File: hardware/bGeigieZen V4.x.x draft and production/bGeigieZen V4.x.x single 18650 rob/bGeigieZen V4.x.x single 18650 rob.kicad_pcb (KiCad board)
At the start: 2 copper layers, 129.4 x 64.6 mm, 13 parts, among them J1 M5 2x15 pin, J3 GPS, J4 Geiger Safepulse, J5 Extra support header

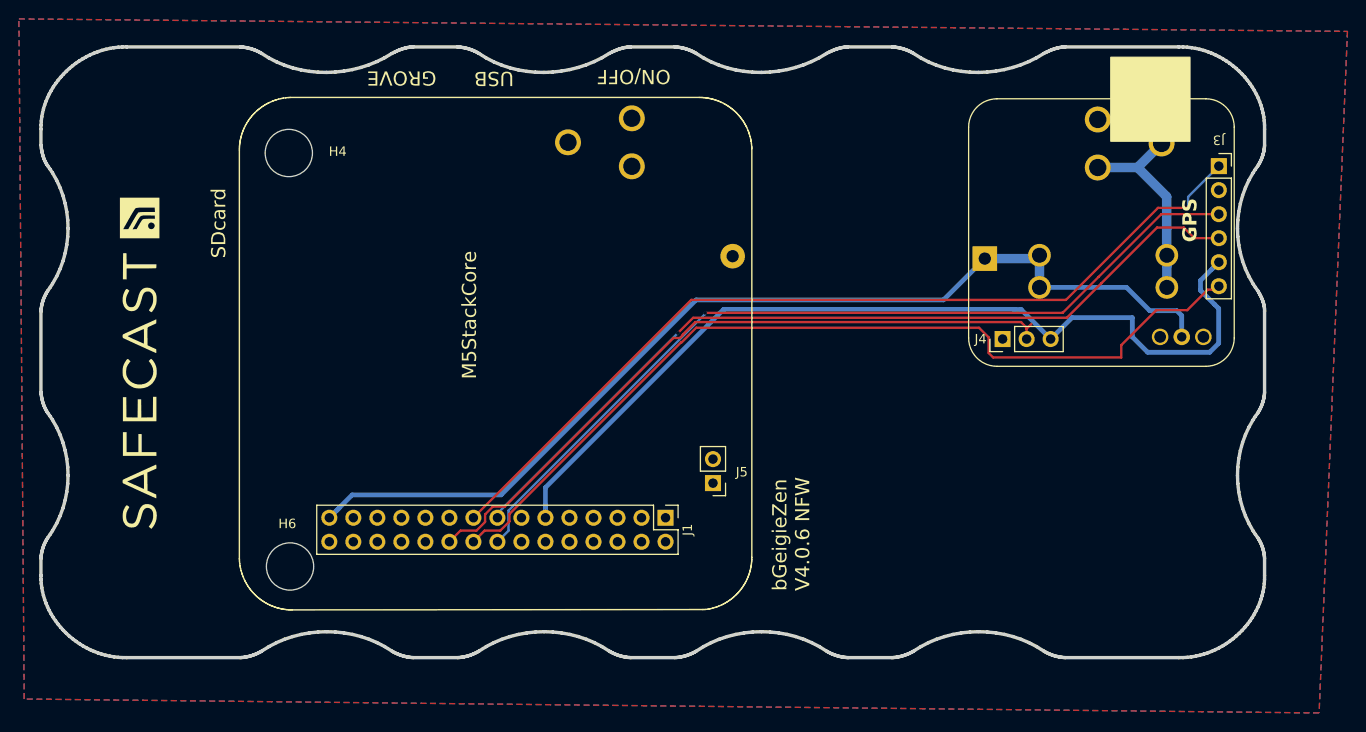
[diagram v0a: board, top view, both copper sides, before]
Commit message: Updated boards for Zen V4.0.7
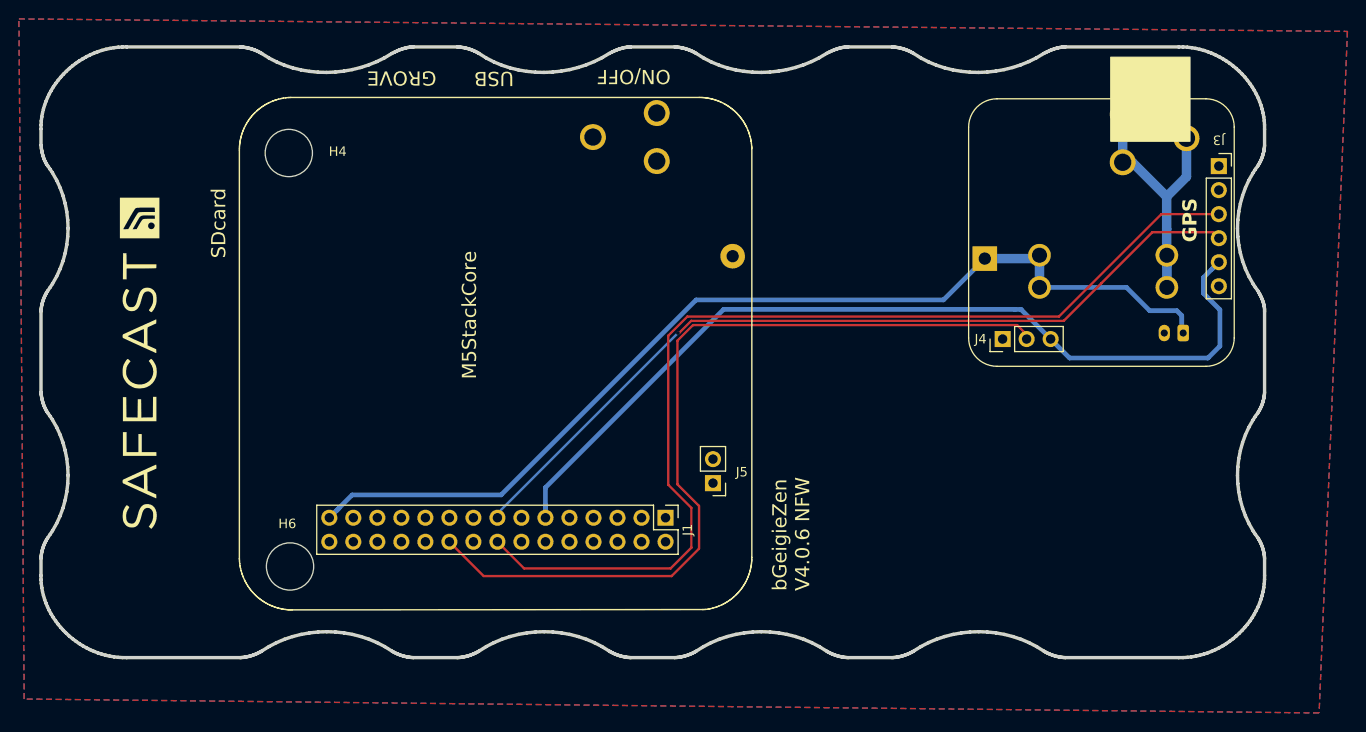
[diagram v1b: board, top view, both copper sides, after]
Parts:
- removed QI charger: QI GND, Connector_JST:JST_PH_B2B-PH-K_1x02_P2.00mm_Vertical
- added QIcharger1: QI GND, Connector_JST:JST_PH_B2B-PH-K_1x02_P2.00mm_Vertical, B.Cu at (205.4, 96.9)
- moved G*** 3.27 mm to (169.0, 76.8)
- moved BT1 2.70 mm to (175.1, 76.3)
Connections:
- J1 pad 17: /SDA -> unconnected-(J1-Pin_17-Pad17)
- J1 pad 18: /SCL -> unconnected-(J1-Pin_18-Pad18)
- J3 pad 1: /SDA -> unconnected-(J3-Pin_1-Pad1)
- J3 pad 6: /SCL -> unconnected-(J3-Pin_6-Pad6)
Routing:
- net /SCL: track 95.8 -> 0.00 mm
- net /SDA: track 95.1 -> 0.00 mm, vias 1 -> 0
- net /GIO2 on Core and GIO32 on Core-2: track 72.5 -> 91.1 mm
- net /TX2: track 91.1 -> 109.6 mm, vias 1 -> 0
- net 3.3V: track 100.0 -> 97.6 mm
- net Net-(BT1-+): track 32.9 -> 30.7 mm
- net unconnected-(J1-Pin_18-Pad18): track 0.00 -> 1.69 mm
- net unconnected-(J3-Pin_6-Pad6): track 0.00 -> 0.52 mm

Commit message: Updated 3D models sizes
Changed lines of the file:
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@@
 		(model "${KIPRJMOD}/shapes3D/lnd7318-2.wrl"
 			(offset
-				(xyz -15.5 -32.5 -9)
+				(xyz -17 -34 -9)
 			)
 			(scale
-				(xyz 3.5 3.5 3.5)
+				(xyz 3.9 3.9 3.9)
 			)
 			(rotate
-				(xyz 90 0 -125)
+				(xyz 90 -0 -125)
 			)
 		)
 		(model "${KIPRJMOD}/shapes3D/grid cover.wrl"
 			(offset
-				(xyz -15 -32.5 -16)
+				(xyz -17 -34 -16)
 			)
 			(scale
-				(xyz 0.32 0.32 0.32)
+				(xyz 0.38 0.38 0.38)
 			)
 			(rotate
-				(xyz 0 -180 55)
+				(xyz -0 -180 55)
 			)
 		)
@@
 	)
 	(gr_rect
-		(start 197.724724 67.751456)
-		(end 206.106724 76.641456)
+		(start 202.1078 69.2684)
+		(end 210.4898 74.2684)
 		(locked yes)
 		(stroke

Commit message: Added 3d update 3dModel of tube grid and update boards
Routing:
- net /BAT: track 109.7 -> 109.2 mm
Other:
- board text added: "bGeigieZen V4.0.7 NFW"
- board text removed: "bGeigieZen V4.0.6 NFW"
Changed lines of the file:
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@@
 (kicad_pcb
-	(version 20240703)
+	(version 20240706)
 	(generator "pcbnew")
 	(generator_version "8.99")
@@
 	(paper "A4")
 	(title_block
-		(title "bGeigieZen Draft V4.0.6 NFW")
-		(date "2024-06-20")
-		(rev "V4.0.6 rob")
+		(title "bGeigieZen Draft V4.0.7 NFW")
+		(date "2024-07-27")
+		(rev "V4.0.7 rob")
 		(comment 1 "Not For Whimps version.")
 	)
@@
 			(layer "F.SilkS")
 		)
+		(embedded_fonts no)
 	)
 	(footprint "Connector_PinHeader_2.54mm:PinHeader_2x15_P2.54mm_Vertical"
@@
 			(pintype "passive")
 		)
+		(embedded_fonts no)
 		(model "${KICAD6_3DMODEL_DIR}/Connector_PinHeader_2.54mm.3dshapes/PinHeader_2x15_P2.54mm_Vertical.wrl"
 			(offset
@@
 			(pintype "passive")
 		)
+		(embedded_fonts no)
 		(model "${KICAD8_3DMODEL_DIR}/Connector_PinHeader_2.54mm.3dshapes/PinHeader_1x06_P2.54mm_Vertical.step"
 			(offset
@@
 			(layers "F&B.Cu" "*.Mask")
 		)
+		(embedded_fonts no)
 	)
 	(footprint "Connector_PinHeader_2.54mm:PinHeader_1x02_P2.54mm_Vertical"
@@
 			(pintype "passive")
 		)
+		(embedded_fonts no)
 		(model "${KICAD6_3DMODEL_DIR}/Connector_PinHeader_2.54mm.3dshapes/PinHeader_1x02_P2.54mm_Vertical.wrl"
 			(hide yes)
@@
 			(pintype "passive")
 		)
+		(embedded_fonts no)
 		(model "${KICAD6_3DMODEL_DIR}/Connector_PinHeader_2.54mm.3dshapes/PinHeader_1x03_P2.54mm_Vertical.wrl"
 			(hide yes)
@@
 			(layers "F&B.Cu" "*.Mask")
 		)
+		(embedded_fonts no)
 	)
 	(footprint "Diode_THT:D_DO-201_P15.24mm_Horizontal"
@@
 			(pintype "passive")
 		)
+		(embedded_fonts no)
 		(model "${KICAD8_3DMODEL_DIR}/Diode_THT.3dshapes/D_DO-201_P15.24mm_Horizontal.wrl"
 			(offset
@@
 			)
 		)
+		(embedded_fonts no)
 	)
 	(footprint "Library:BATTERY_18650-HOLDER"
@@
 			(net 1 "GND")
 		)
+		(embedded_fonts no)
 		(model "${KIPRJMOD}/shapes3D/KEYELCO_54.wrl"
 			(offset
@@
 			(solder_mask_margin 0.102)
 		)
+		(embedded_fonts no)
 		(model "${KIPRJMOD}/shapes3D/Fuse - mini 10A v005.wrl"
 			(offset
@@
 			(layer "B.SilkS")
 		)
+		(embedded_fonts no)
 	)
 	(footprint "Connector_JST:JST_PH_B2B-PH-K_1x02_P2.00mm_Vertical"
@@
 			(pintype "passive")
 		)
+		(embedded_fonts no)
 		(model "${KICAD8_3DMODEL_DIR}/Connector_JST.3dshapes/JST_PH_B2B-PH-K_1x02_P2.00mm_Vertical.wrl"
 			(offset
@@
 		(layer "Edge.Cuts")
 	)
-	(gr_text "bGeigieZen\nV4.0.6 NFW"
+	(gr_text "bGeigieZen\nV4.0.7 NFW"
 		(at 200.5584 112.724 90)
 		(layer "B.SilkS")
@@
 		)
 	)
-	(gr_text "bGeigieZen\nV4.0.6 NFW\n"
+	(gr_text "bGeigieZen\nV4.0.7 NFW\n"
 		(at 163.9316 124.2048 90)
 		(layer "F.SilkS")
@@
 	)
 	(segment
-		(start 209.155 86.9507)
-		(end 209.155 87.0096)
+		(start 196.704 91.6855)
+		(end 192.7543 95.6352)
 		(width 0.25)
 		(layer "F.Cu")
@@
 	)
 	(segment
-		(start 209.155 86.9065)
-		(end 209.155 86.8991)
+		(start 209.155 86.9507)
+		(end 209.155 87.0096)
 		(width 0.25)
 		(layer "F.Cu")
@@
 	)
 	(segment
-		(start 202.1323 86.2572)
-		(end 208.5186 86.2572)
+		(start 153.2328 95.6352)
+		(end 151.943 96.925)
 		(width 0.25)
 		(layer "F.Cu")
@@
 	)
 	(segment
-		(start 152.068404 96.9252)
-		(end 151.943 96.9252)
+		(start 209.155 86.9065)
+		(end 209.155 86.8991)
 		(width 0.25)
 		(layer "F.Cu")
@@
 	)
 	(segment
+		(start 208.2034 86.8918)
+		(end 207.5688 86.2572)
+		(width 0.25)
+		(layer "F.Cu")
+		(net 2)
+	)
+	(segment
+		(start 202.1323 86.2572)
+		(end 196.704 91.6855)
+		(width 0.25)
+		(layer "F.Cu")
+		(net 2)
+	)
+	(segment
 		(start 209.155 86.9212)
 		(end 209.155 86.9065)
@@
 	)
 	(segment
-		(start 209.1551 86.8935)
-		(end 209.1551 86.8918)
+		(start 151.943 96.925)
+		(end 151.943 96.9252)
 		(width 0.25)
 		(layer "F.Cu")
@@
 	)
 	(segment
-		(start 196.704 91.6855)
-		(end 192.7543 95.6352)
+		(start 192.7543 95.6352)
+		(end 153.2328 95.6352)
+		(width 0.25)
+		(layer "F.Cu")
+		(net 2)
+	)
+	(segment
+		(start 209.1551 86.8935)
+		(end 209.1551 86.8918)
 		(width 0.25)
 		(layer "F.Cu")
@@
 	)
 	(segment
-		(start 153.358404 95.6352)
-		(end 152.068404 96.9252)
+		(start 209.155 86.8936)
+		(end 209.155 86.8954)
 		(width 0.25)
 		(layer "F.Cu")
@@
 	(segment
 		(start 209.155 86.8936)
-		(end 209.155 86.8954)
+		(end 209.1551 86.8935)
 		(width 0.25)
 		(layer "F.Cu")
@@
 	)
 	(segment
-		(start 196.748 91.642)
-		(end 196.704 91.6855)
+		(start 207.5688 86.2572)
+		(end 202.1323 86.2572)
 		(width 0.25)
 		(layer "F.Cu")
@@
 	)
 	(segment
-		(start 209.155 86.8936)
-		(end 209.1551 86.8935)
+		(start 209.1551 86.8918)
+		(end 208.2034 86.8918)
 		(width 0.25)
 		(layer "F.Cu")
@@
 	)
 	(segment
-		(start 192.7543 95.6352)
-		(end 153.358404 95.6352)
-		(width 0.25)
-		(layer "F.Cu")
-		(net 2)
-	)
-	(segment
-		(start 196.704 91.6855)
-		(end 202.1323 86.2572)
-		(width 0.25)
-		(layer "F.Cu")
-		(net 2)
-	)
-	(segment
 		(start 209.155 86.9507)
 		(end 209.155 86.9212)
@@
 		(net 2)
 	)
-	(segment
-		(start 208.5186 86.2572)
-		(end 209.155 86.8936)
-		(width 0.25)
-		(layer "F.Cu")
-		(net 2)
-	)
 	(via
 		(at 151.943 96.9252)
@@
 	)
 	(segment
-		(start 116.156 115.382)
-		(end 115.796 115.742)
-		(width 0.5)
-		(layer "B.Cu")
-		(net 27)
-	)
-	(segment
 		(start 133.2482 114.045)
 		(end 117.4929 114.045)
@@
 		)
 	)
+	(embedded_fonts no)
 )

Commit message: Some more small fixes on the V4.x.x NFW board
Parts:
- renumbered QIcharger1 to QI-charger
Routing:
- net Net-(BT1-+): track 30.7 -> 32.9 mm
- net /TX2: track 109.6 -> 110.7 mm
- net 3.3V: track 97.6 -> 96.7 mm
- net /GIO2 on Core and GIO32 on Core-2: track 91.1 -> 91.7 mm

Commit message: Updated boards
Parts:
- moved Fuse 2A 0.12 mm to (197.0, 90.4)
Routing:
- net Net-(BT1-+): track 32.9 -> 30.7 mm
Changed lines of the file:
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@@
 	(footprint "bGeigieZen:FUSE_3557-2"
 		(layer "B.Cu")
-		(at 196.9222 90.3992 180)
+		(at 197.0426 90.3992 180)
 		(property "Reference" "Fuse 2A"
 			(at 0.0722 -4.24 0)
@@
 		)
 		(pad "1" thru_hole circle
-			(at -6.735 -1.7 180)
-			(size 2.4 2.4)
-			(drill 1.6)
+			(at -7 -1.7 180)
+			(size 2.6 2.6)
+			(drill 1.8)
 			(layers "F&B.Cu" "*.Mask")
 			(remove_unused_layers no)
@@
 		)
 		(pad "1" thru_hole circle
-			(at -6.735 1.7 180)
-			(size 2.4 2.4)
-			(drill 1.6)
+			(at -7 1.7 180)
+			(size 2.6 2.6)
+			(drill 1.8)
 			(layers "F&B.Cu" "*.Mask")
 			(remove_unused_layers no)
@@
 		)
 		(pad "2" thru_hole circle
-			(at 6.735 -1.7 180)
-			(size 2.4 2.4)
-			(drill 1.6)
+			(at 7 -1.7 180)
+			(size 2.6 2.6)
+			(drill 1.8)
 			(layers "F&B.Cu" "*.Mask")
 			(remove_unused_layers no)
@@
 		)
 		(pad "2" thru_hole circle
-			(at 6.735 1.7 180)
-			(size 2.4 2.4)
-			(drill 1.6)
+			(at 7 1.7 180)
+			(size 2.6 2.6)
+			(drill 1.8)
 			(layers "F&B.Cu" "*.Mask")
 			(remove_unused_layers no)
@@
 	)
 	(segment
-		(start 203.657 88.7161)
-		(end 203.657 88.7076)
-		(width 0.5)
-		(layer "B.Cu")
-		(net 31)
-	)
-	(segment
-		(start 203.657 89.7863)
-		(end 203.657 89.2427)
-		(width 0.5)
-		(layer "B.Cu")
-		(net 31)
-	)
-	(segment
-		(start 205.736 78.3616)
-		(end 205.736 80.3974)
-		(width 1)
-		(layer "B.Cu")
-		(net 31)
-	)
-	(segment
-		(start 203.657 89.7865)
-		(end 203.657 89.7863)
+		(start 204.0426 92.0992)
+		(end 204.0426 88.6992)
 		(width 1)
 		(layer "B.Cu")
@@
 	)
 	(segment
-		(start 203.657 88.835)
-		(end 203.657 88.7671)
-		(width 0.5)
-		(layer "B.Cu")
-		(net 31)
-	)
-	(segment
 		(start 205.7356 78.3612)
 		(end 205.7356 76.3258)
@@
 	)
 	(segment
-		(start 203.657 88.7161)
-		(end 203.657 88.7076)
-		(width 1)
-		(layer "B.Cu")
-		(net 31)
-	)
-	(segment
-		(start 203.657 88.835)
-		(end 203.657 88.7671)
-		(width 1)
-		(layer "B.Cu")
-		(net 31)
-	)
-	(segment
-		(start 203.657 88.7331)
-		(end 203.657 88.7161)
-		(width 0.5)
-		(layer "B.Cu")
-		(net 31)
-	)
-	(segment
-		(start 203.636 85.899)
-		(end 203.636 82.497)
-		(width 1)
-		(layer "B.Cu")
-		(net 31)
-	)
-	(segment
-		(start 203.657 88.7076)
-		(end 203.657 88.6992)
-		(width 1)
-		(layer "B.Cu")
-		(net 31)
-	)
-	(segment
-		(start 203.657 88.7331)
-		(end 203.657 88.7161)
-		(width 1)
-		(layer "B.Cu")
-		(net 31)
-	)
-	(segment
-		(start 203.636 85.899)
-		(end 203.657 85.9202)
-		(width 0.5)
-		(layer "B.Cu")
-		(net 31)
-	)
-	(segment
-		(start 203.6572 88.7074)
-		(end 203.6572 88.6992)
-		(width 0.5)
-		(layer "B.Cu")
-		(net 31)
-	)
-	(segment
-		(start 203.657 88.7671)
-		(end 203.657 88.7331)
-		(width 1)
-		(layer "B.Cu")
-		(net 31)
-	)
-	(segment
-		(start 203.657 85.9202)
-		(end 203.657 88.6992)
-		(width 0.5)
-		(layer "B.Cu")
-		(net 31)
-	)
-	(segment
-		(start 203.636 87.6052)
-		(end 203.636 85.899)
-		(width 1)
-		(layer "B.Cu")
-		(net 31)
-	)
-	(segment
-		(start 203.657 89.2427)
-		(end 203.657 88.9709)
-		(width 1)
-		(layer "B.Cu")
-		(net 31)
-	)
-	(segment
-		(start 203.657 88.9709)
-		(end 203.657 88.835)
-		(width 0.5)
-		(layer "B.Cu")
-		(net 31)
-	)
-	(segment
-		(start 203.657 89.7863)
-		(end 203.657 89.2427)
-		(width 1)
-		(layer "B.Cu")
-		(net 31)
-	)
-	(segment
 		(start 205.736 78.3616)
 		(end 205.7356 78.3612)
@@
 	)
 	(segment
-		(start 203.657 90.9428)
-		(end 203.6572 90.943)
-		(width 0.5)
-		(layer "B.Cu")
-		(net 31)
-	)
-	(segment
-		(start 203.657 89.7865)
-		(end 203.657 89.7863)
-		(width 0.5)
+		(start 205.736 78.3616)
+		(end 205.736 82.2274)
+		(width 1)
 		(layer "B.Cu")
 		(net 31)
@@
 	)
 	(segment
-		(start 203.657 88.7671)
-		(end 203.657 88.7331)
-		(width 0.5)
-		(layer "B.Cu")
-		(net 31)
-	)
-	(segment
-		(start 203.657 88.9709)
-		(end 203.657 88.835)
+		(start 204.0426 83.9208)
+		(end 204.0426 88.6992)
 		(width 1)
 		(layer "B.Cu")
@@
 	)
 	(segment
-		(start 200.005 78.8658)
-		(end 203.636 82.497)
-		(width 1)
-		(layer "B.Cu")
-		(net 31)
-	)
-	(segment
-		(start 205.736 80.3974)
-		(end 203.636 82.497)
-		(width 1)
-		(layer "B.Cu")
-		(net 31)
-	)
-	(segment
-		(start 203.6572 90.943)
-		(end 203.6572 92.0992)
-		(width 0.5)
-		(layer "B.Cu")
-		(net 31)
-	)
-	(segment
-		(start 203.657 90.9428)
-		(end 203.657 89.7865)
+		(start 205.736 82.2274)
+		(end 204.0426 83.9208)
 		(width 1)
 		(layer "B.Cu")
@@
 	)
 	(segment
-		(start 203.657 89.2427)
-		(end 203.657 88.9709)
-		(width 0.5)
-		(layer "B.Cu")
-		(net 31)
-	)
-	(segment
-		(start 203.657 88.7076)
-		(end 203.657 88.6992)
-		(width 0.5)
-		(layer "B.Cu")
-		(net 31)
-	)
-	(segment
-		(start 203.657 92.0992)
-		(end 203.657 90.9428)
+		(start 198.9876 78.8658)
+		(end 204.0426 83.9208)
 		(width 1)
 		(layer "B.Cu")
 		(net 31)
-	)
-	(segment
-		(start 203.657 88.7076)
-		(end 203.6572 88.7074)
-		(width 0.5)
-		(layer "B.Cu")
-		(net 31)
